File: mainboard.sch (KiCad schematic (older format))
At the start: 44 parts

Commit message: Changed UC to ATxmega128A1U (TQFP100) which has more pins.
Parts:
- removed IC?: ATXMEGA256A3U-A, TQFP64, symbol ATXMEGA256A3U-A
- added C? (x7): 100n, ~, symbol C
- added IC?: ATXMEGA128A1U-A, TQFP100, symbol ATXMEGA128A1U-A
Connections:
- wire segments 162 -> 157
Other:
- note added: "Todo: Connector\n"
- note removed: "USB"
- moved on the sheet: C?, D?, J?, K?, P?, R?, RV?, U?A

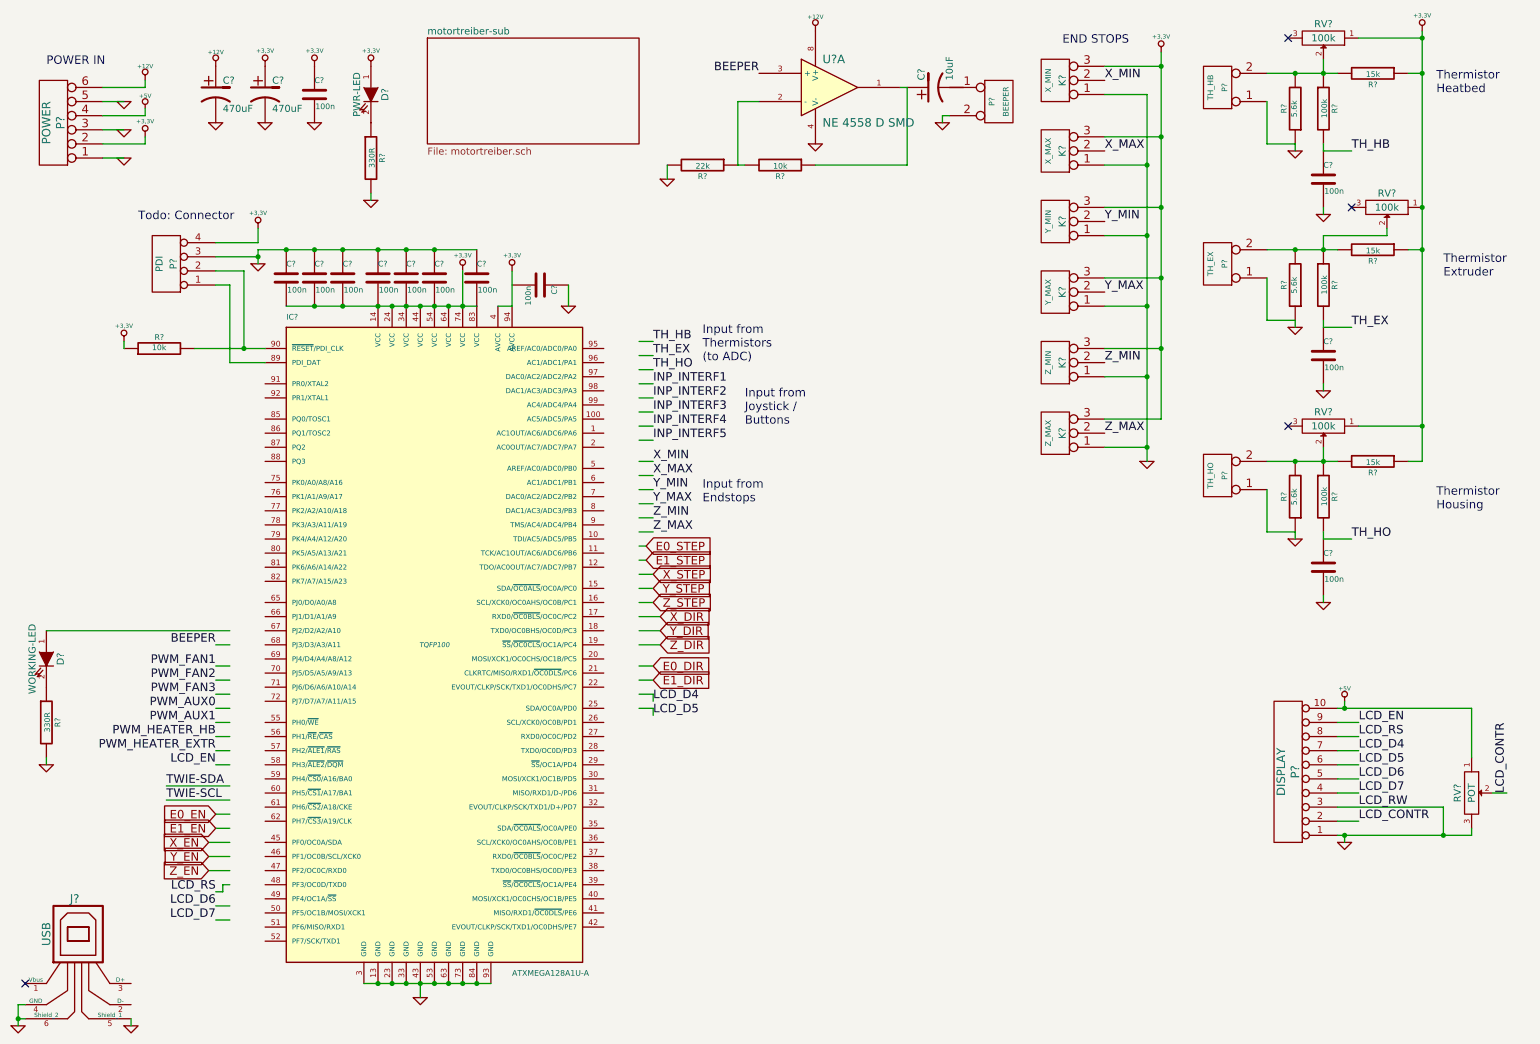
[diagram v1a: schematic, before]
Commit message: Added USART and I2C connectors, reworked pin mappings for new UC
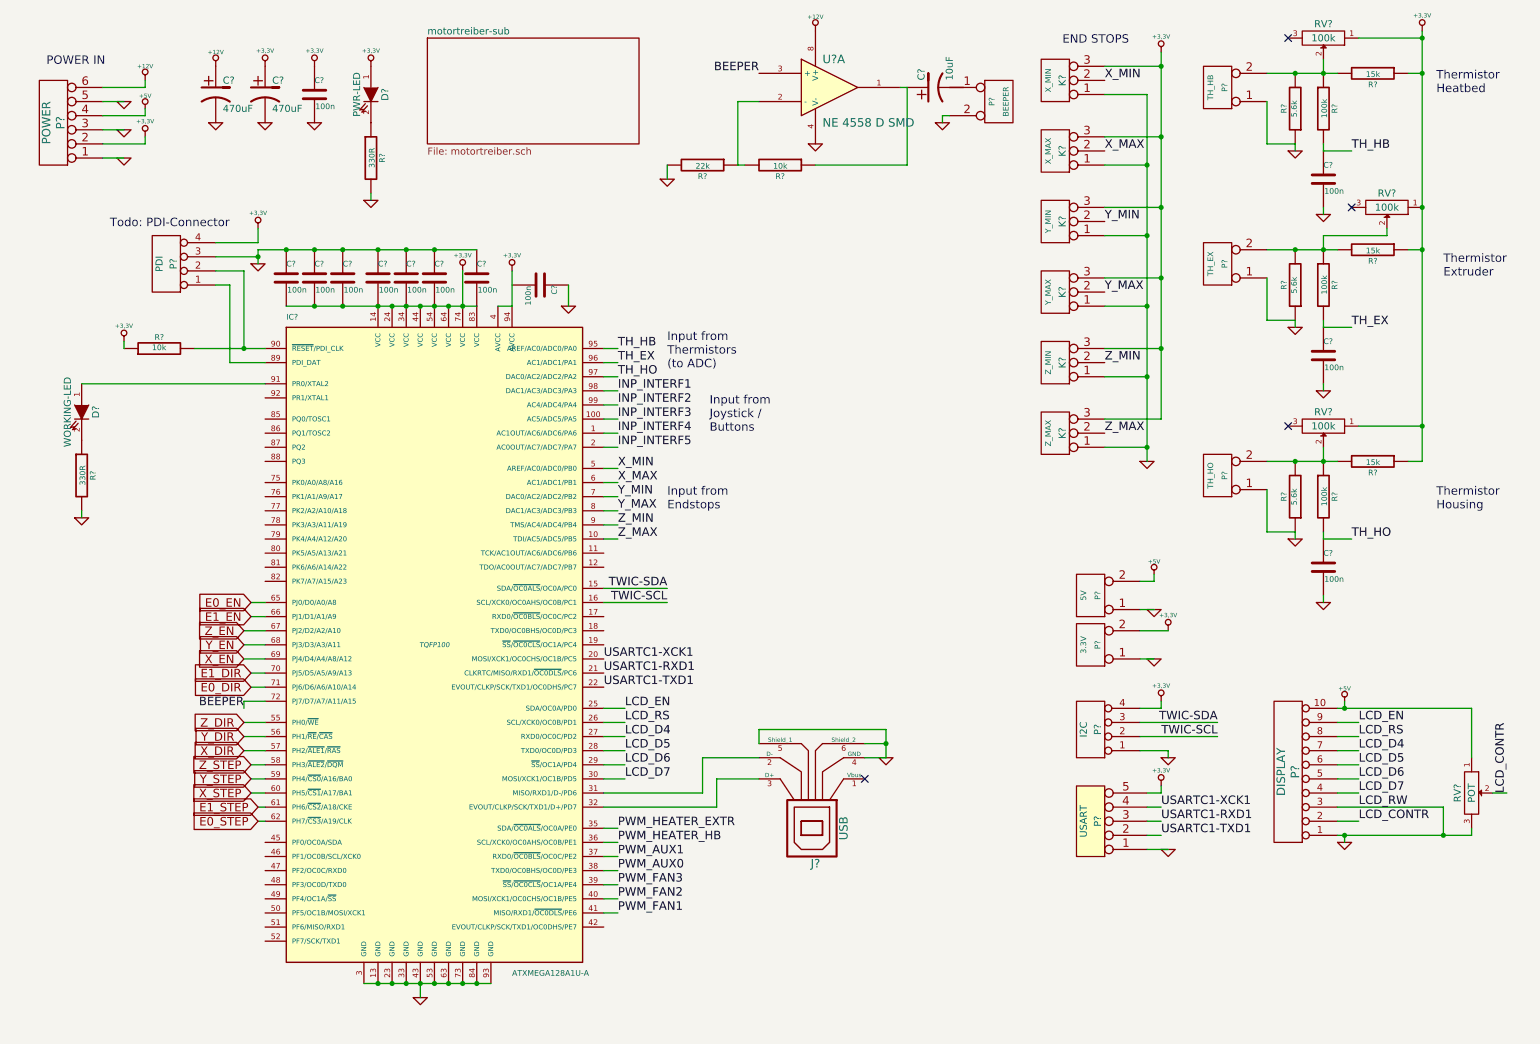
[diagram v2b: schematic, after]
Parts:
- added P?: I2C, symbol CONN_4
- added P?: USART, symbol CONN_5
- added P?: 3.3V, symbol CONN_2
- added P?: 5V, symbol CONN_2
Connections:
- net labels added: TWIC-SCL, TWIC-SDA, USARTC1-RXD1, USARTC1-TXD1, USARTC1-XCK1
- net labels removed: TWIE-SCL, TWIE-SDA
- wire segments 157 -> 178
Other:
- note added: "Todo: PDI-Connector\n"
- note removed: "Todo: Connector\n"
- moved on the sheet: D?, J?, R?

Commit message: Added schematic for pwm-drivers. Added ULN 2003 as low current driver.
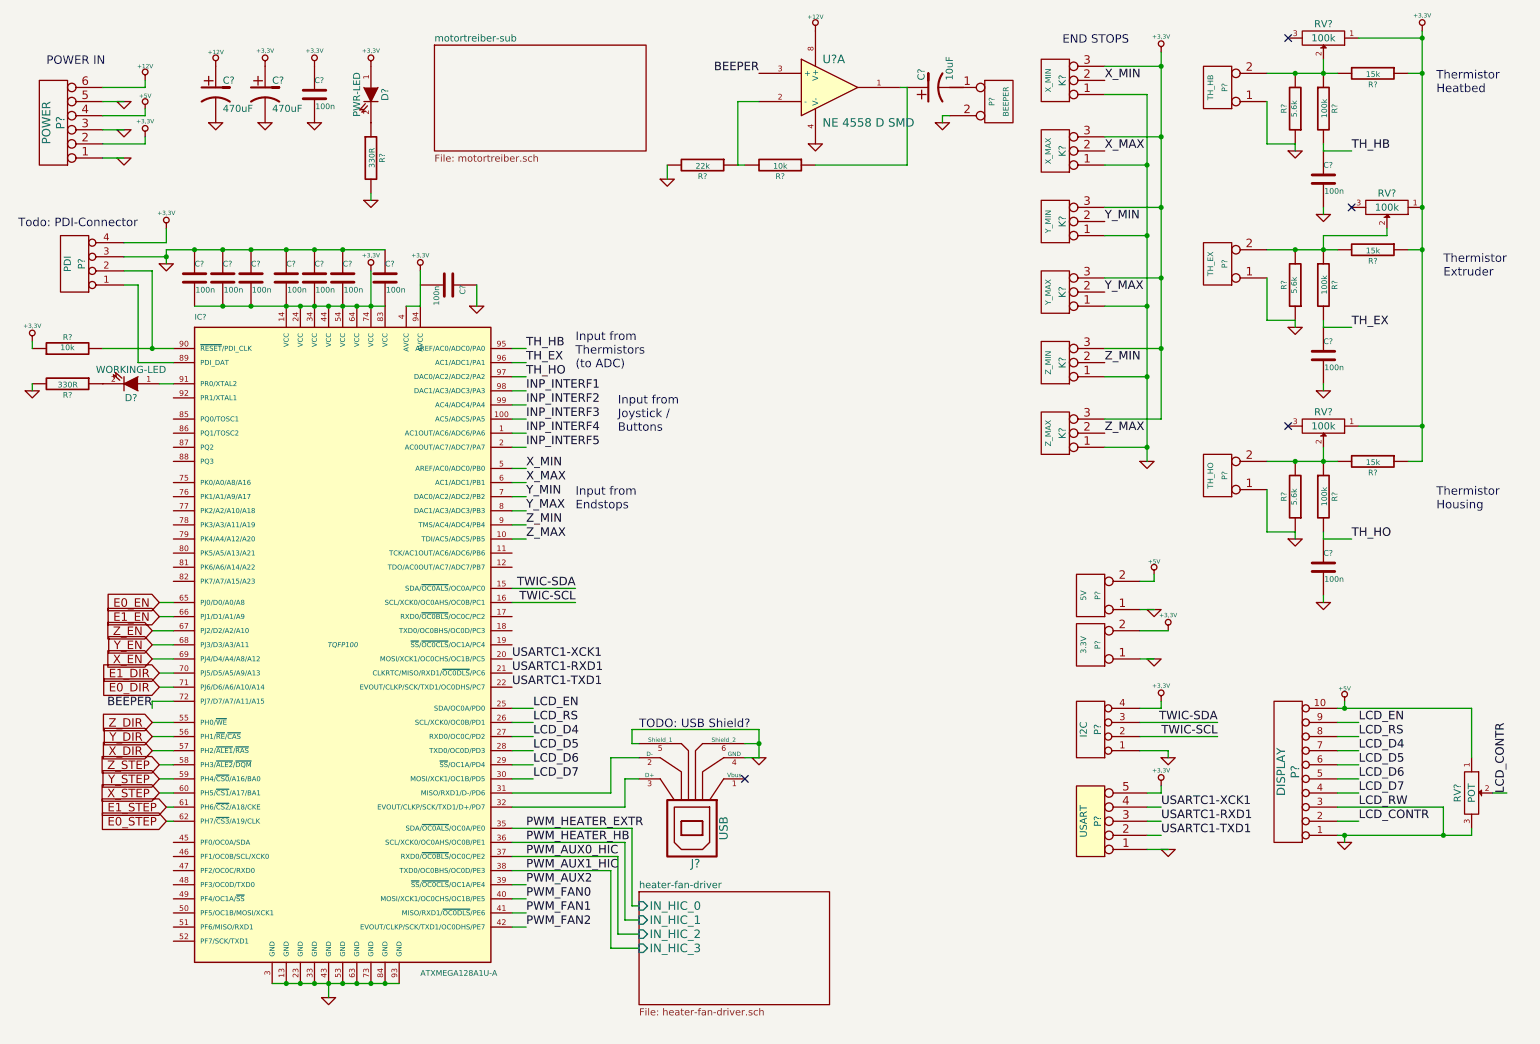
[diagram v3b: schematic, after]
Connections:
- net PWM_FAN2: now also IC?.42 (EVOUT/CLKP/SCK/TXD1/OC0DHS/PE7); no longer IC?.40 (MOSI/XCK1/OC0CHS/OC1B/PE5)
- net PWM_AUX0 renamed PWM_AUX1_HIC
- net PWM_AUX1 renamed PWM_AUX0_HIC
- net PWM_FAN3 renamed PWM_AUX2
- new net PWM_FAN0: IC?.40 (MOSI/XCK1/OC0CHS/OC1B/PE5)
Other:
- note added: "TODO: USB Shield?"
- moved on the sheet: C?, D?, IC?, J?, P?, R?

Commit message: Added 12V-connector. Changed LCD connector to 14-pin (including d0-d7 now)
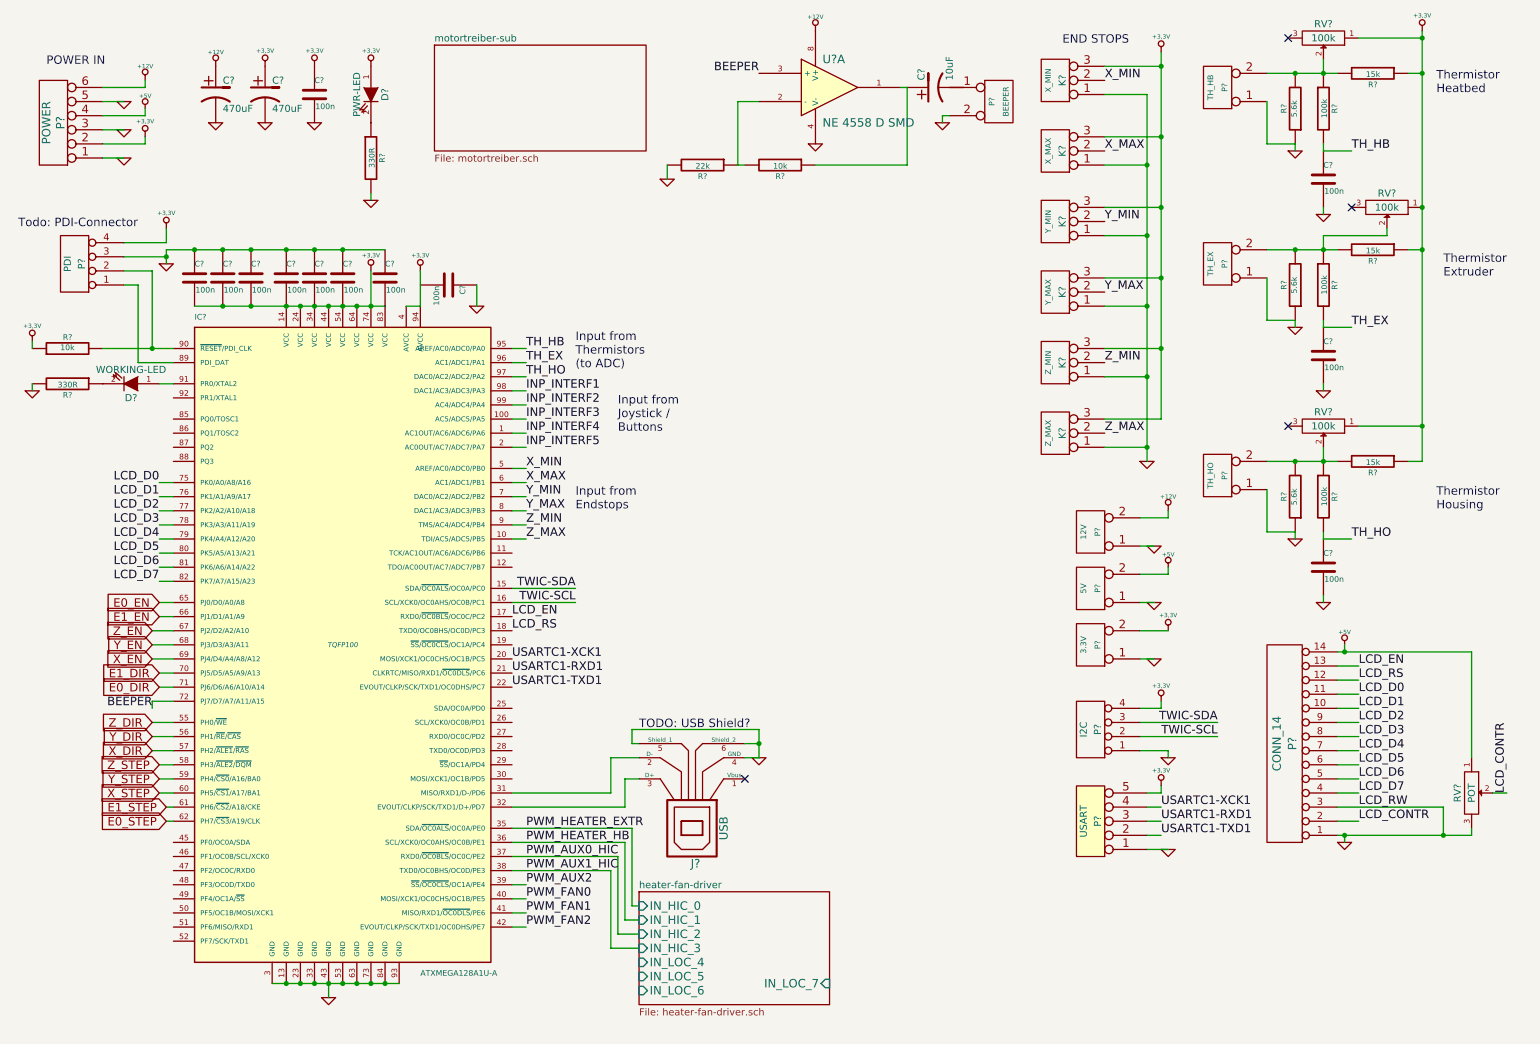
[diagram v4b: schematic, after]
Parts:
- removed P?: DISPLAY, symbol CONN_10
- added P?: CONN_14, symbol CONN_14
- added P?: 5V, symbol CONN_2
- P?: value 5V -> 12V
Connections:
- net +12V: now also P?.2 (PM)
- net +5V: now also P?.14 (P14), P?.2 (PM); no longer P?.2 (PM)
- net GND: now also P?.1 (P1), P?.1 (P1), P?.3 (P3)
- net LCD_CONTR: now also P?.2 (P2)
- net LCD_D4: now also IC?.79 (PK4/A4/A12/A20), P?.7 (P7); no longer IC?.27 (RXD0/OC0C/PD2)
- net LCD_D5: now also IC?.80 (PK5/A5/A13/A21), P?.6 (P6); no longer IC?.28 (TXD0/OC0D/PD3)
- net LCD_D6: now also IC?.81 (PK6/A6/A14/A22), P?.5 (P5); no longer IC?.29 (~SS~/OC1A/PD4)
- net LCD_D7: now also IC?.82 (PK7/A7/A15/A23), P?.4 (P4); no longer IC?.30 (MOSI/XCK1/OC1B/PD5)
- net LCD_EN: now also IC?.17 (RXD0/~OC0BLS~/OC0C/PC2), P?.13 (P13); no longer IC?.25 (SDA/OC0A/PD0)
- net LCD_RS: now also IC?.18 (TXD0/OC0BHS/OC0D/PC3), P?.12 (P12); no longer IC?.26 (SCL/XCK0/OC0B/PD1)
- net LCD_D0: now reaches IC?.75 (PK0/A0/A8/A16)
- net LCD_D0: now also P?.11 (P11)
- net LCD_D1: now reaches IC?.76 (PK1/A1/A9/A17)
- net LCD_D1: now also P?.10 (P10)
- net LCD_D2: now reaches IC?.77 (PK2/A2/A10/A18)
- net LCD_D2: now also P?.9 (P9)
- net LCD_D3: now reaches IC?.78 (PK3/A3/A11/A19)
- net LCD_D3: now also P?.8 (P8)
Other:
- moved on the sheet: P?
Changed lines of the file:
@@
 Text Label 1550 5450 2    60   ~ 0
 BEEPER
-Text Label 4250 5650 0    60   ~ 0
+Text Label 1600 4250 2    60   ~ 0
 LCD_D4
-Text Label 4250 5750 0    60   ~ 0
+Text Label 1600 4350 2    60   ~ 0
 LCD_D5
-Text Label 4250 5850 0    60   ~ 0
+Text Label 1600 4450 2    60   ~ 0
 LCD_D6
-Text Label 4250 5950 0    60   ~ 0
+Text Label 1600 4550 2    60   ~ 0
 LCD_D7
-Text Label 4250 5550 0    60   ~ 0
+Text Label 4100 4900 0    60   ~ 0
 LCD_RS
-Text Label 4250 5450 0    60   ~ 0
+Text Label 4100 4800 0    60   ~ 0
 LCD_EN
 $Comp
@@
 $EndComp
 $Comp
-L CONN_10 P?
-U 1 1 53347A6B
-P 9600 5900
-F 0 "P?" V 9550 5900 60  0000 C CNN
-F 1 "DISPLAY" V 9650 5900 60  0000 C CNN
-F 2 "" H 9600 5900 60  0000 C CNN
-F 3 "" H 9600 5900 60  0000 C CNN
-	1    9600 5900
-	-1   0    0    1
-$EndComp
-$Comp
 L GND #PWR?
 U 1 1 53347A82
@@
 L +5V #PWR?
 U 1 1 53347B2B
-P 10000 5400
-F 0 "#PWR?" H 10000 5490 20  0001 C CNN
-F 1 "+5V" H 10000 5490 30  0000 C CNN
-F 2 "" H 10000 5400 60  0000 C CNN
-F 3 "" H 10000 5400 60  0000 C CNN
-	1    10000 5400
-	1    0    0    -1
-$EndComp
-Text Label 10100 5650 0    60   ~ 0
+P 10000 5000
+F 0 "#PWR?" H 10000 5090 20  0001 C CNN
+F 1 "+5V" H 10000 5090 30  0000 C CNN
+F 2 "" H 10000 5000 60  0000 C CNN
+F 3 "" H 10000 5000 60  0000 C CNN
+	1    10000 5000
+	1    0    0    -1
+$EndComp
+Text Label 10100 5250 0    60   ~ 0
 LCD_RS
-Text Label 10100 5550 0    60   ~ 0
+Text Label 10100 5150 0    60   ~ 0
 LCD_EN
 Text Label 10100 5750 0    60   ~ 0
@@
 	9950 6350 10900 6350
 Wire Wire Line
-	10000 5400 10000 5450
-Wire Wire Line
-	9950 5450 10900 5450
+	10000 5000 10000 5050
 Wire Wire Line
 	9950 5550 10100 5550
@@
 Wire Wire Line
 	10100 6050 9950 6050
-Connection ~ 10000 5450
+Connection ~ 10000 5050
 Wire Wire Line
 	9950 6150 10700 6150
@@
 	9950 6250 10100 6250
 Wire Wire Line
-	10900 5450 10900 5800
+	10900 5050 10900 5800
 Wire Wire Line
 	10900 6350 10900 6300
@@
 	9450 1450 9650 1450
 Wire Wire Line
-	10450 950  10550 950
+	10550 950  10450 950
 Wire Wire Line
 	9650 2750 9650 2700
@@
 	4100 6150 4900 6150
 Wire Wire Line
-	4250 5450 4100 5450
-Wire Wire Line
-	4100 5550 4250 5550
-Wire Wire Line
-	4100 5650 4250 5650
-Wire Wire Line
-	4100 5750 4250 5750
-Wire Wire Line
-	4100 5850 4250 5850
-Wire Wire Line
-	4100 5950 4250 5950
-Wire Wire Line
 	1550 5450 1550 5400
 Wire Wire Line
@@
 L CONN_2 P?
 U 1 1 534D73F4
-P 8200 4650
-F 0 "P?" V 8150 4650 40  0000 C CNN
-F 1 "5V" V 8250 4650 40  0000 C CNN
-F 2 "" H 8200 4650 60  0000 C CNN
-F 3 "" H 8200 4650 60  0000 C CNN
-	1    8200 4650
+P 8200 4200
+F 0 "P?" V 8150 4200 40  0000 C CNN
+F 1 "12V" V 8250 4200 40  0000 C CNN
+F 2 "" H 8200 4200 60  0000 C CNN
+F 3 "" H 8200 4200 60  0000 C CNN
+	1    8200 4200
 	-1   0    0    1
 $EndComp
@@
 L GND #PWR?
 U 1 1 534D740E
-P 8650 4750
-F 0 "#PWR?" H 8650 4750 30  0001 C CNN
-F 1 "GND" H 8650 4680 30  0001 C CNN
-F 2 "" H 8650 4750 60  0000 C CNN
-F 3 "" H 8650 4750 60  0000 C CNN
-	1    8650 4750
-	1    0    0    -1
-$EndComp
-Wire Wire Line
-	8650 4750 8550 4750
+P 8650 4300
+F 0 "#PWR?" H 8650 4300 30  0001 C CNN
+F 1 "GND" H 8650 4230 30  0001 C CNN
+F 2 "" H 8650 4300 60  0000 C CNN
+F 3 "" H 8650 4300 60  0000 C CNN
+	1    8650 4300
+	1    0    0    -1
+$EndComp
+Wire Wire Line
+	8650 4300 8550 4300
 $Comp
 L GND #PWR?
@@
 	1    0    0    -1
 $EndComp
-$Comp
-L +5V #PWR?
-U 1 1 534D77C2
-P 8650 4500
-F 0 "#PWR?" H 8650 4590 20  0001 C CNN
-F 1 "+5V" H 8650 4590 30  0000 C CNN
-F 2 "" H 8650 4500 60  0000 C CNN
-F 3 "" H 8650 4500 60  0000 C CNN
-	1    8650 4500
-	1    0    0    -1
-$EndComp
-Wire Wire Line
-	8650 4550 8550 4550
-Wire Wire Line
-	8650 4550 8650 4500
 Wire Wire Line
 	8750 4900 8550 4900
@@
 F4 "IN_HIC_2" I L 5000 7050 60
 F5 "IN_HIC_3" I L 5000 7150 60
+F6 "IN_LOC_4" I L 5000 7250 60
+F7 "IN_LOC_5" I L 5000 7350 60
+F8 "IN_LOC_6" I L 5000 7450 60
+F9 "IN_LOC_7" I R 6350 7400 60
 $EndSheet
 Wire Wire Line
@@
 Wire Wire Line
 	4800 7150 5000 7150
+Wire Wire Line
+	1600 4550 1700 4550
+Wire Wire Line
+	1600 4450 1700 4450
+Wire Wire Line
+	1600 4350 1700 4350
+Wire Wire Line
+	1600 4250 1700 4250
+Text Label 1600 4150 2    60   ~ 0
+LCD_D3
+Wire Wire Line
+	1600 4150 1700 4150
+Text Label 1600 4050 2    60   ~ 0
+LCD_D2
+Text Label 1600 3950 2    60   ~ 0
+LCD_D1
+Text Label 1600 3850 2    60   ~ 0
+LCD_D0
+Wire Wire Line
+	1600 3850 1700 3850
+Wire Wire Line
+	1600 3950 1700 3950
+Wire Wire Line
+	1600 4050 1700 4050
+$Comp
+L CONN_14 P?
+U 1 1 534FCF38
+P 9600 5700
+F 0 "P?" V 9570 5700 60  0000 C CNN
+F 1 "CONN_14" V 9680 5700 60  0000 C CNN
+F 2 "" H 9600 5700 60  0000 C CNN
+F 3 "" H 9600 5700 60  0000 C CNN
+	1    9600 5700
+	-1   0    0    1
+$EndComp
+Wire Wire Line
+	9950 5050 10900 5050
+Wire Wire Line
+	10100 5150 9950 5150
+Wire Wire Line
+	9950 5250 10100 5250
+Text Label 10100 5350 0    60   ~ 0
+LCD_D0
+Text Label 10100 5450 0    60   ~ 0
+LCD_D1
+Text Label 10100 5550 0    60   ~ 0
+LCD_D2
+Text Label 10100 5650 0    60   ~ 0
+LCD_D3
+Wire Wire Line
+	9950 5350 10100 5350
+Wire Wire Line
+	9950 5450 10100 5450
+$Comp
+L CONN_2 P?
+U 1 1 534FD85E
+P 8200 4600
+F 0 "P?" V 8150 4600 40  0000 C CNN
+F 1 "5V" V 8250 4600 40  0000 C CNN
+F 2 "" H 8200 4600 60  0000 C CNN
+F 3 "" H 8200 4600 60  0000 C CNN
+	1    8200 4600
+	-1   0    0    1
+$EndComp
+$Comp
+L GND #PWR?
+U 1 1 534FD864
+P 8650 4700
+F 0 "#PWR?" H 8650 4700 30  0001 C CNN
+F 1 "GND" H 8650 4630 30  0001 C CNN
+F 2 "" H 8650 4700 60  0000 C CNN
+F 3 "" H 8650 4700 60  0000 C CNN
+	1    8650 4700
+	1    0    0    -1
+$EndComp
+Wire Wire Line
+	8650 4700 8550 4700
+$Comp
+L +5V #PWR?
+U 1 1 534FD86B
+P 8750 4450
+F 0 "#PWR?" H 8750 4540 20  0001 C CNN
+F 1 "+5V" H 8750 4540 30  0000 C CNN
+F 2 "" H 8750 4450 60  0000 C CNN
+F 3 "" H 8750 4450 60  0000 C CNN
+	1    8750 4450
+	1    0    0    -1
+$EndComp
+Wire Wire Line
+	8550 4500 8750 4500
+Wire Wire Line
+	8750 4500 8750 4450
+Wire Wire Line
+	8550 4100 8750 4100
+Wire Wire Line
+	8750 4100 8750 4050
+$Comp
+L +12V #PWR?
+U 1 1 534FDEC7
+P 8750 4050
+F 0 "#PWR?" H 8750 4000 20  0001 C CNN
+F 1 "+12V" H 8750 4150 30  0000 C CNN
+F 2 "" H 8750 4050 60  0000 C CNN
+F 3 "" H 8750 4050 60  0000 C CNN
+	1    8750 4050
+	1    0    0    -1
+$EndComp
 $EndSCHEMATC
